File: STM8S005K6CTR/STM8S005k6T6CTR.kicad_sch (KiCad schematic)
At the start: 22 parts, among them IC1 STM8S005K6T6CTR, IC2 LM2671M-5.0_NOPB, J1 282837-2, J2 Conn_01x04_Pin, J3 Conn_01x03_Pin, J4 Conn_01x08_Pin, J5 Conn_01x06_Pin, Y1 8 MHz

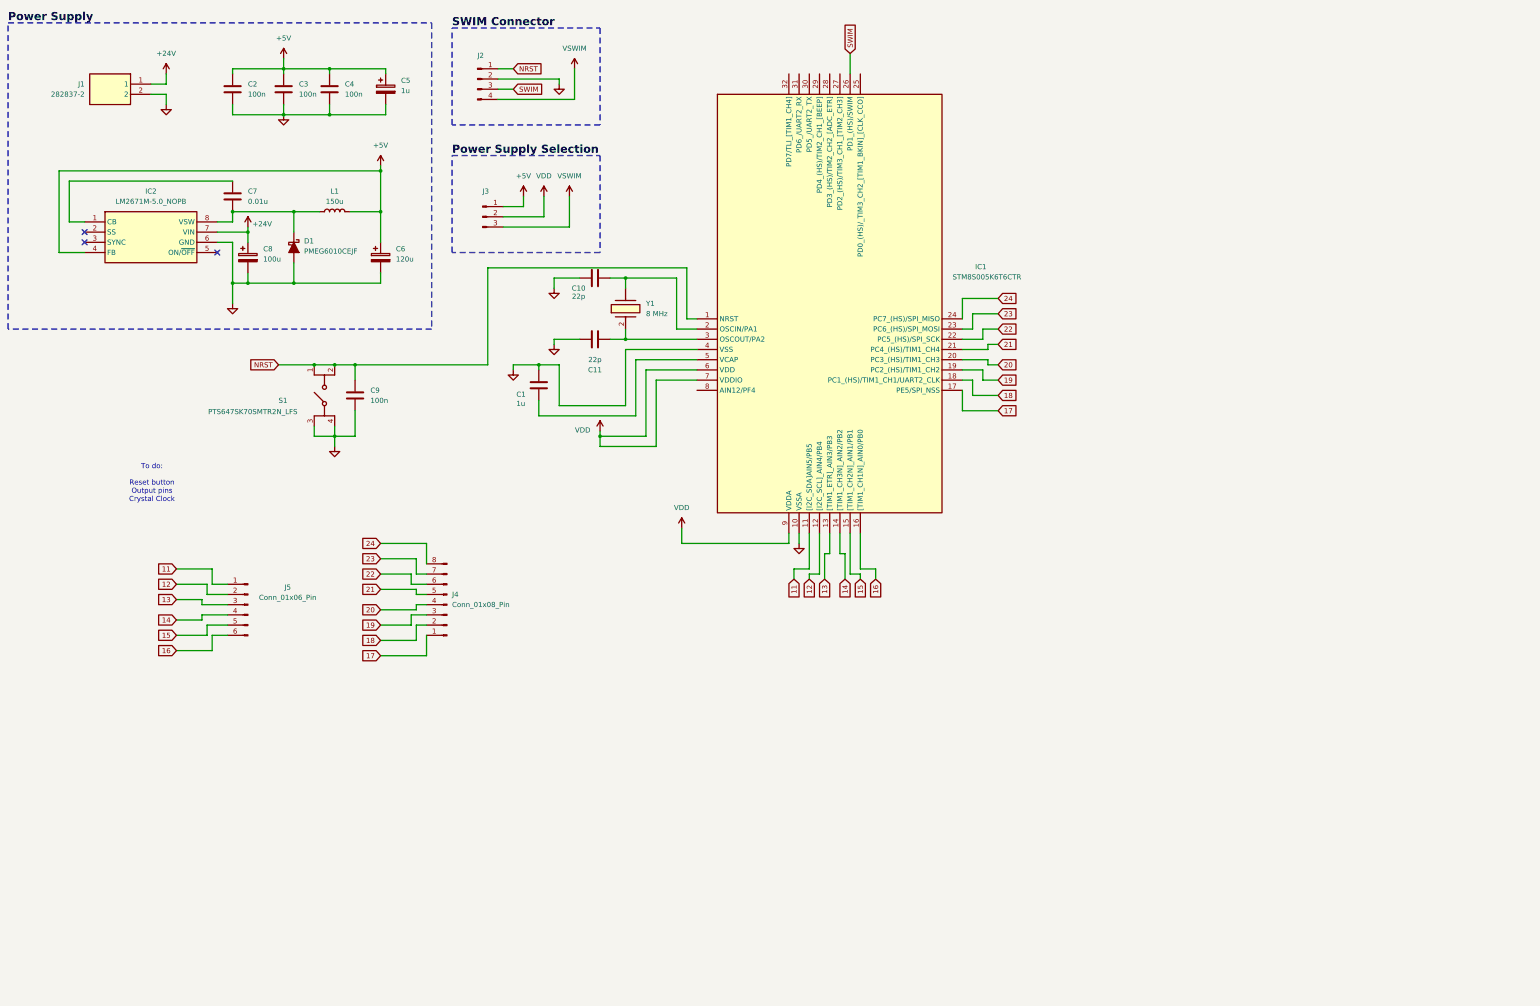
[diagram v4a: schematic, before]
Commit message: [STM8S005K6T6CTR] Board scheme: Improvements
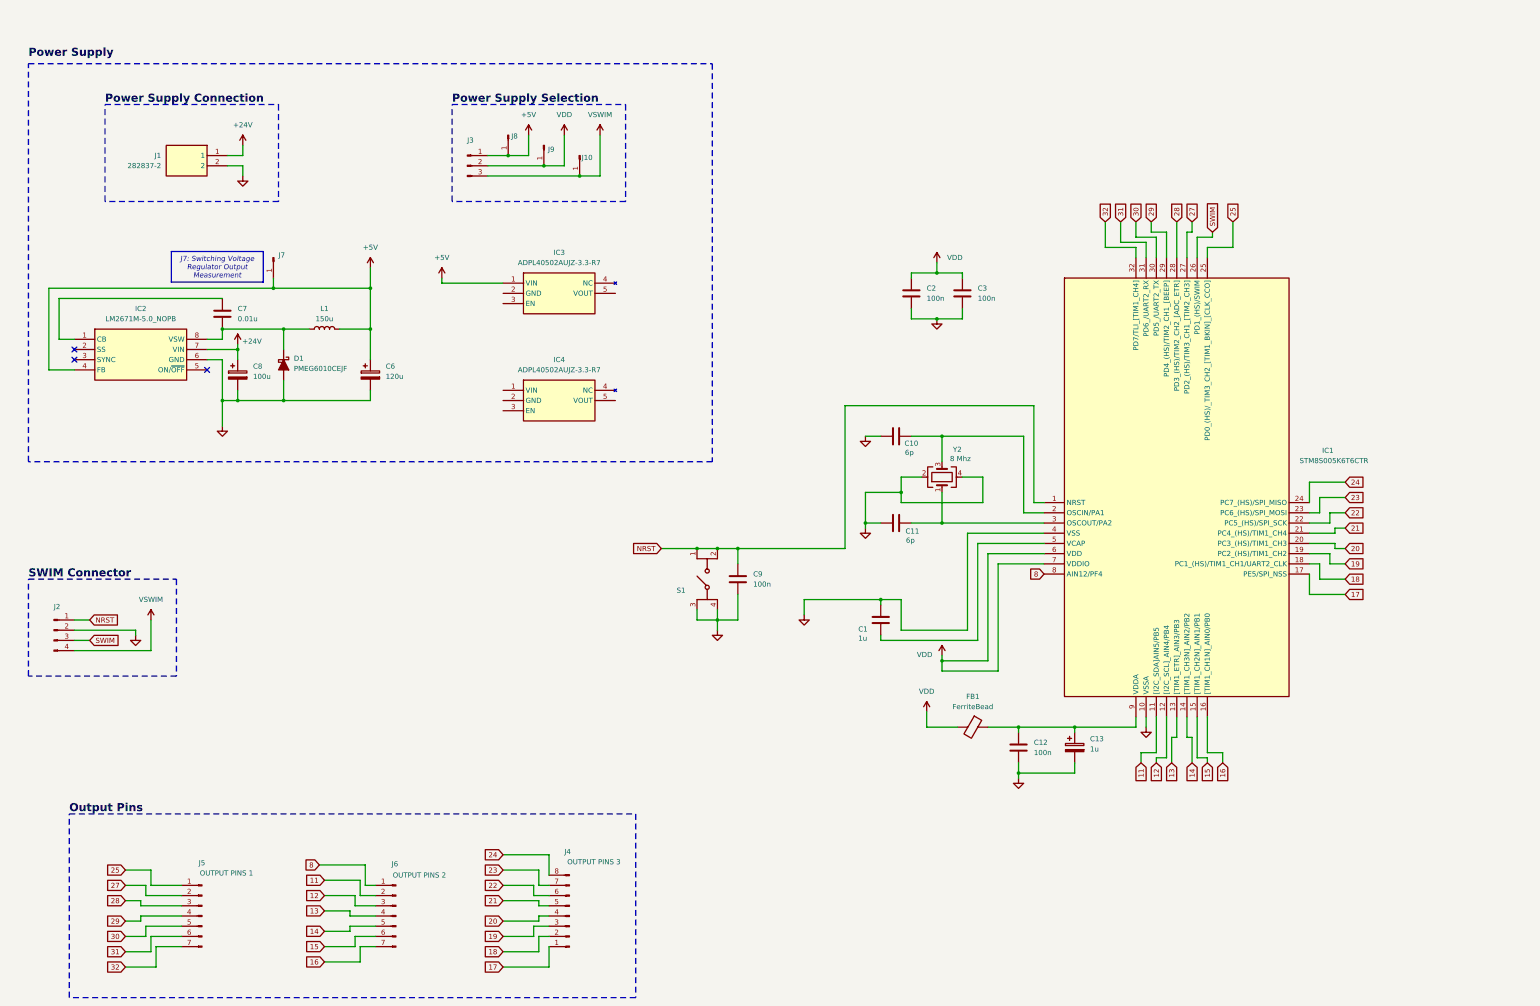
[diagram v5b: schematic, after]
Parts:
- removed C4: 100n, Capacitor_SMD:C_0805_2012Metric, symbol Device:C
- removed C5: 1u, Capacitor_THT:CP_Radial_D5.0mm_P2.00mm, symbol Device:C_Polarized
- removed J5: Conn_01x06_Pin, symbol Connector:Conn_01x06_Pin
- removed Y1: 8 MHz, 830029914_Wurth_8Mhz:830029914, symbol 830029914:830029914
- added C12: 100n, Capacitor_SMD:C_0805_2012Metric, symbol Device:C
- added C13: 1u, Capacitor_THT:CP_Radial_D5.0mm_P2.00mm, symbol Device:C_Polarized
- added FB1: FerriteBead, Resistor_SMD:R_0603_1608Metric, symbol Device:FerriteBead
- added IC3, IC4: ADPL40502AUJZ-3.3-R7, SOT95P280X100-5N, symbol ADPL40502AUJZ-3_3-R7:ADPL40502AUJZ-3.3-R7
- added J10, J7, J8, J9: Conn_01x01_Pin, Connector_PinHeader_2.54mm:PinHeader_1x01_P2.54mm_Vertical, symbol Connector:Conn_01x01_Pin
- added J5, J6: Conn_01x07_Pin, Connector_PinSocket_2.54mm:PinSocket_1x07_P2.54mm_Vertical, symbol Connector:Conn_01x07_Pin
- added Y2: 8 Mhz, ECS-80-33820-CVY-TR3:ECS80833B2QCVYTR3, symbol Device:Crystal_GND24
- C10, C11: value 22p -> 6p
- J4: footprint (none) -> Connector_PinSocket_2.54mm:PinSocket_1x08_P2.54mm_Vertical
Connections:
- net +5V: now also IC3.1 (VIN), J7.1 (Pin_1), J8.1 (Pin_1); no longer C2.1, C3.1
- net 11: now also J6.2 (Pin_2)
- net 12: now also J6.3 (Pin_3)
- net 13: now also J6.4 (Pin_4)
- net 14: now also J6.5 (Pin_5)
- net 15: now also J6.6 (Pin_6)
- net 16: now also J6.7 (Pin_7)
- net GND: now also C12.2, C13.2, Y2.2, Y2.4
- net VDD: now also C2.1, C3.1, FB1.2, J9.1 (Pin_1); no longer IC1.9 (VDDA)
- net VSWIM: now also J10.1 (Pin_1)
- net at C10.1, IC1.2 (OSCIN/PA1): now also Y2.3
- net at C11.1, IC1.3 (OSCOUT/PA2): now also Y2.1
- net 25: now reaches IC1.25 (PD0_(HS)/_TIM3_CH2_[TIM1_BKIN]_[CLK_CCO])
- net 25: now also J5.1 (Pin_1)
- net 27: now reaches IC1.27 (PD2_(HS)/TIM3_CH1_[TIM2_CH3])
- net 27: now also J5.2 (Pin_2)
- net 28: now reaches IC1.28 (PD3_(HS)/TIM2_CH2_[ADC_ETR])
- net 28: now also J5.3 (Pin_3)
- net 29: now reaches IC1.29 (PD4_(HS)/TIM2_CH1_[BEEP])
- net 29: now also J5.4 (Pin_4)
- net 30: now reaches IC1.30 (PD5_/UART2_TX)
- net 30: now also J5.5 (Pin_5)
- net 31: now reaches IC1.31 (PD6_/UART2_RX)
- net 31: now also J5.6 (Pin_6)
- net 32: now reaches IC1.32 (PD7/TLI_[TIM1_CH4])
- net 32: now also J5.7 (Pin_7)
- net 8: now reaches IC1.8 (AIN12/PF4)
- net 8: now also J6.1 (Pin_1)
- new net: C12.1, C13.1, FB1.1, IC1.9 (VDDA)
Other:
- note added: "J7: Switching Voltage Regulator Output Measurement"
- note removed: "To do: Reset button Output pins Crystal Clock"
- moved on the sheet: C1, C10, C11, C2, C3, C6, C7, C8, C9, D1, IC1, IC2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

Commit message: [STM8S005K6T6CTR] Board scheme: Footprints layout. Crystal routing.
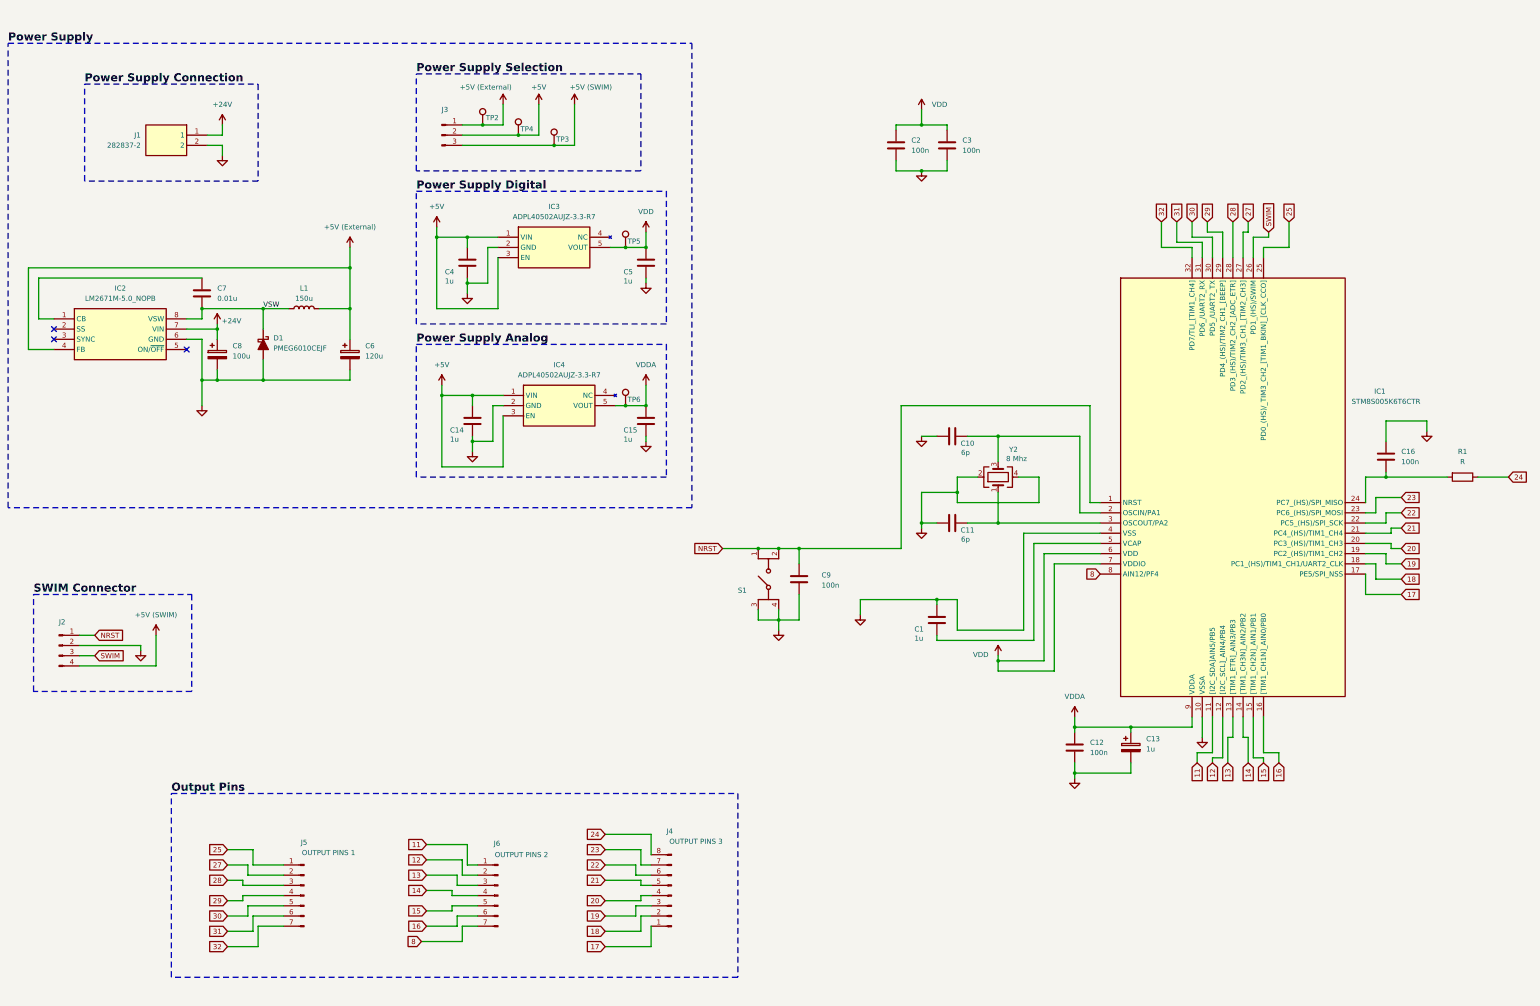
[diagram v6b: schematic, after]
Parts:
- removed FB1: FerriteBead, Resistor_SMD:R_0603_1608Metric, symbol Device:FerriteBead
- removed J10, J7, J8, J9: Conn_01x01_Pin, Connector_PinHeader_2.54mm:PinHeader_1x01_P2.54mm_Vertical, symbol Connector:Conn_01x01_Pin
- added C14, C15, C4, C5: 1u, Capacitor_SMD:C_0603_1608Metric, symbol Device:C
- added C16: 100n, Capacitor_SMD:C_0603_1608Metric, symbol Device:C
- added R1: R, symbol Device:R
- added TP2, TP3, TP4, TP5, TP6: TestPoint, TestPoint:TestPoint_Pad_D1.5mm, symbol Connector:TestPoint
- C10, C11: footprint (none) -> Capacitor_SMD:C_0402_1005Metric
- C12, C2, C3, C9: footprint Capacitor_SMD:C_0805_2012Metric -> Capacitor_SMD:C_0603_1608Metric
- C13: footprint Capacitor_THT:CP_Radial_D5.0mm_P2.00mm -> Capacitor_SMD:C_1210_3225Metric
- IC3, IC4: footprint SOT95P280X100-5N -> ADPL40502AUJZ-3.3-R7:SOT95P280X100-5N
- J2: footprint (none) -> Connector_PinHeader_2.54mm:PinHeader_1x04_P2.54mm_Vertical
- J3: footprint (none) -> Connector_PinHeader_2.54mm:PinHeader_1x03_P2.54mm_Vertical
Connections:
- net +5V: now also IC3.3 (EN), IC4.1 (VIN), IC4.3 (EN), J3.2 (Pin_2), C14.1, C4.1, TP4.1; no longer C6.1, IC2.4 (FB), J3.1 (Pin_1), L1.2
- net 11: now also J6.1 (Pin_1); no longer J6.2 (Pin_2)
- net 12: now also J6.2 (Pin_2); no longer J6.3 (Pin_3)
- net 13: now also J6.3 (Pin_3); no longer J6.4 (Pin_4)
- net 14: now also J6.4 (Pin_4); no longer J6.5 (Pin_5)
- net 15: now also J6.5 (Pin_5); no longer J6.6 (Pin_6)
- net 16: now also J6.6 (Pin_6); no longer J6.7 (Pin_7)
- net 24: now also R1.1; no longer IC1.24 (PC7_(HS)/SPI_MISO)
- net 8: now also J6.7 (Pin_7); no longer J6.1 (Pin_1)
- net GND: now also IC3.2 (GND), IC4.2 (GND), C14.2, C15.2, C16.1, C4.2, C5.2
- net VDD: now also IC3.5 (VOUT), C5.1, TP5.1; no longer J3.2 (Pin_2)
- net VDDA: now reaches C12.1, C13.1, IC1.9 (VDDA)
- net VDDA: now also IC4.5 (VOUT), C15.1, TP6.1
- net VSW: now reaches C7.1, D1.1 (K), IC2.8 (VSW), L1.1
- net VSWIM renamed +5V (SWIM)
- net +5V (SWIM): now also TP3.1
- new net: C16.2, IC1.24 (PC7_(HS)/SPI_MISO), R1.2
- new net +5V (External): C6.1, IC2.4 (FB), J3.1 (Pin_1), L1.2, TP2.1
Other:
- note removed: "J7: Switching Voltage Regulator Output Measurement"
- moved on the sheet: C1, C10, C12, C13, C2, C3, C6, C7, C8, C9, D1, IC1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
